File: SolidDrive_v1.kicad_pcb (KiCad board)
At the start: 2 copper layers, 50 x 70 mm, 13 parts, among them J1 Batt, M1 Motor_DC, Q1 NMOS, Q2 NMOS, Q3 NMOS, Q4 NMOS, U1 LM7805_TO220, U2 TLP250, U3 TLP250, U4 TLP250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

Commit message: [update] complete power cuircuit
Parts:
- added C3: 0.1μF, Capacitor_THT:C_Disc_D3.0mm_W1.6mm_P2.50mm, F.Cu at (67.5, 99.8)
- added C4: 0.1μF, Capacitor_THT:C_Disc_D3.0mm_W1.6mm_P2.50mm, F.Cu at (102.8, 100.2)
- added C5: 0.1μF, Capacitor_THT:C_Disc_D3.0mm_W1.6mm_P2.50mm, F.Cu at (67.2, 118.2)
- added C6: 0.1μF, Capacitor_THT:C_Disc_D3.0mm_W1.6mm_P2.50mm, F.Cu at (103.2, 117.8)
- added C7: 470μF, Capacitor_THT:CP_Radial_D5.0mm_P2.00mm, F.Cu at (52.8, 64.2)
- added C8: 470μF, Capacitor_THT:CP_Radial_D5.0mm_P2.00mm, F.Cu at (58.5, 64.2)
- added D1: 1N4007, Diode_THT:D_DO-41_SOD81_P10.16mm_Horizontal, F.Cu at (65.8, 84.0)
- added D2: 1N4007, Diode_THT:D_DO-41_SOD81_P10.16mm_Horizontal, F.Cu at (103.8, 83.8)
- added D3: 1N4007, Diode_THT:D_DO-41_SOD81_P10.16mm_Horizontal, F.Cu at (107.8, 101.5)
- added D4: 1N4007, Diode_THT:D_DO-41_SOD81_P10.16mm_Horizontal, F.Cu at (54.2, 102.0)
- added R1: R_PullDown, Resistor_THT:R_Axial_DIN0207_L6.3mm_D2.5mm_P10.16mm_Horizontal, F.Cu at (72.1, 92.8)
- added R2: R_PullDown, Resistor_THT:R_Axial_DIN0207_L6.3mm_D2.5mm_P10.16mm_Horizontal, F.Cu at (89.7, 93.2)
- added R3: R_PullDown, Resistor_THT:R_Axial_DIN0207_L6.3mm_D2.5mm_P10.16mm_Horizontal, F.Cu at (72.6, 96.2)
- added R4: R_PullDown, Resistor_THT:R_Axial_DIN0207_L6.3mm_D2.5mm_P10.16mm_Horizontal, F.Cu at (89.2, 96.8)
- added R5: R_Gate, Resistor_THT:R_Axial_DIN0207_L6.3mm_D2.5mm_P10.16mm_Horizontal, F.Cu at (68.8, 82.7)
- added R6: R_Gate, Resistor_THT:R_Axial_DIN0207_L6.3mm_D2.5mm_P10.16mm_Horizontal, F.Cu at (102.5, 86.8)
- added R7: R_Gate, Resistor_THT:R_Axial_DIN0207_L6.3mm_D2.5mm_P10.16mm_Horizontal, F.Cu at (68.5, 102.9)
- added R8: R_Gate, Resistor_THT:R_Axial_DIN0207_L6.3mm_D2.5mm_P10.16mm_Horizontal, F.Cu at (102.8, 103.9)
- moved M1 47.7 mm to (82.0, 65.0)
- moved C1 42.0 mm to (55.5, 71.0)
- moved Q2 41.3 mm to (95.0, 89.9), turned to 180 degrees
- moved J1 40.7 mm to (72.0, 65.0)
- moved Q4 40.6 mm to (90.0, 99.8)
- moved Q3 40.6 mm to (75.0, 99.5)
- moved Q1 38.9 mm to (80.0, 89.7), turned to 180 degrees
- moved C2 37.4 mm to (55.5, 81.0)
- moved U1 35.4 mm to (60.7, 76.0)
- moved U5 30.7 mm to (105.8, 105.5)
- moved U4 30.0 mm to (105.2, 87.4)
- moved U3 24.9 mm to (57.5, 105.2)
- moved U2 7.39 mm to (58.1, 87.8)
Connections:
- C1 pad 2: GND -> GNDPWR
- C2 pad 2: GND -> GNDPWR
- J1 pad 1: GND -> +BATT
- J1 pad 2: +BATT -> GNDPWR
- Q3 pad 3: GND -> GNDPWR
- Q4 pad 3: GND -> GNDPWR
- U1 pad 2: GND -> GNDPWR
- U2 pad 3: unconnected-(U2-C-Pad3) -> GND
- U2 pad 5: unconnected-(U2-VEE-Pad5) -> Net-(M1-+)
- U2 pad 6: unconnected-(U2-VO-Pad6) -> Net-(R5-Pad2)
- U2 pad 7: unconnected-(U2-VO-Pad7) -> Net-(R5-Pad2)
- U2 pad 8: unconnected-(U2-VCC-Pad8) -> Net-(D1-K)
- U3 pad 3: unconnected-(U3-C-Pad3) -> GND
- U3 pad 5: unconnected-(U3-VEE-Pad5) -> GNDPWR
- U3 pad 6: unconnected-(U3-VO-Pad6) -> Net-(R6-Pad2)
- U3 pad 7: unconnected-(U3-VO-Pad7) -> Net-(R6-Pad2)
- U3 pad 8: unconnected-(U3-VCC-Pad8) -> Net-(D3-K)
- U4 pad 3: unconnected-(U4-C-Pad3) -> GND
- U4 pad 5: unconnected-(U4-VEE-Pad5) -> Net-(M1--)
- U4 pad 6: unconnected-(U4-VO-Pad6) -> Net-(R8-Pad1)
- U4 pad 7: unconnected-(U4-VO-Pad7) -> Net-(R8-Pad1)
- U4 pad 8: unconnected-(U4-VCC-Pad8) -> Net-(D2-K)
- U5 pad 3: unconnected-(U5-C-Pad3) -> GND
- U5 pad 5: unconnected-(U5-VEE-Pad5) -> GNDPWR
- U5 pad 6: unconnected-(U5-VO-Pad6) -> Net-(R7-Pad1)
- U5 pad 7: unconnected-(U5-VO-Pad7) -> Net-(R7-Pad1)
- U5 pad 8: unconnected-(U5-VCC-Pad8) -> Net-(D4-K)
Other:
- board size 50 x 70 mm -> 70 x 70 mm

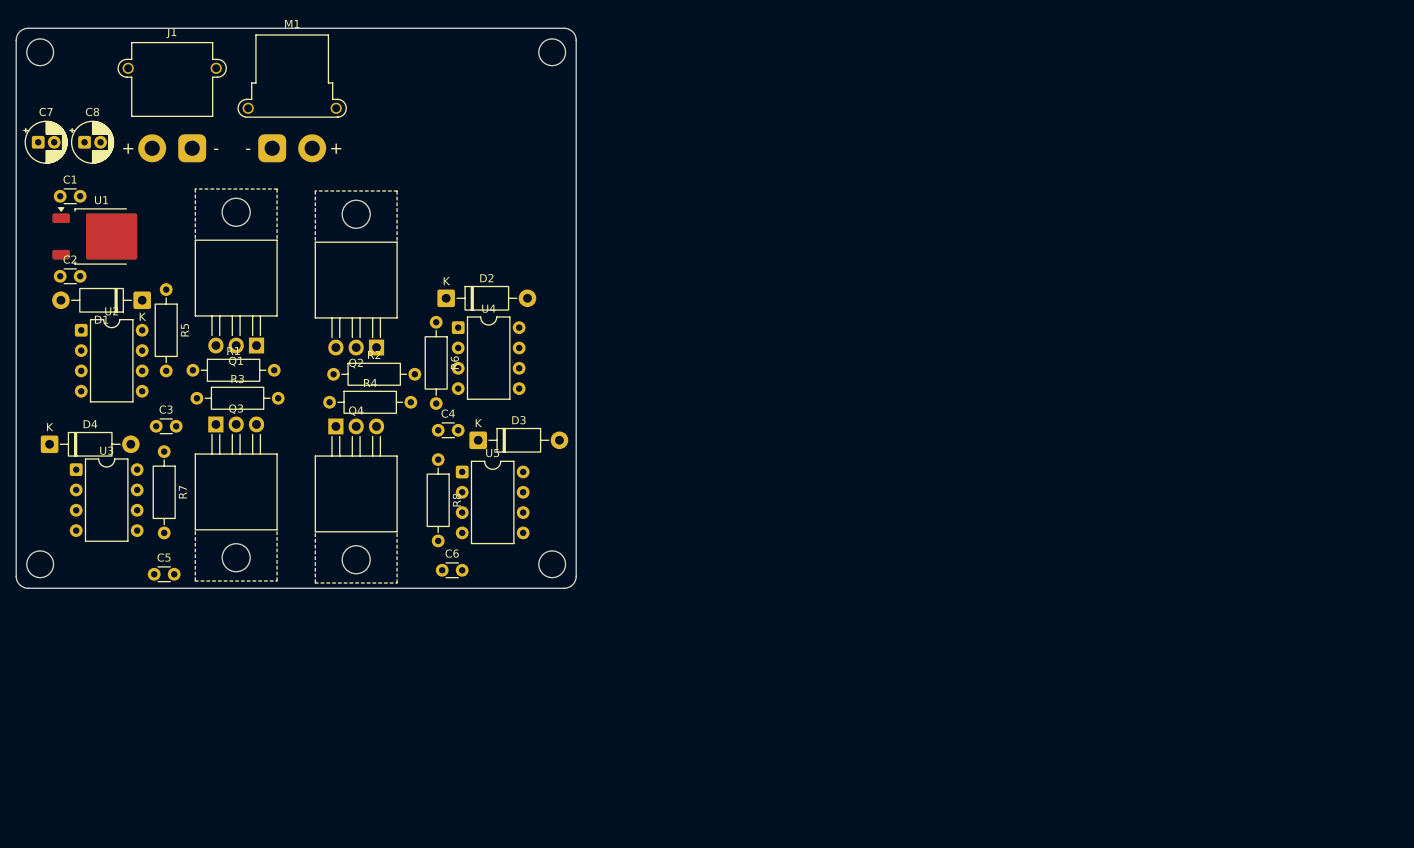
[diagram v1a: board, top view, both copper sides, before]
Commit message: [update] complete logic circuit
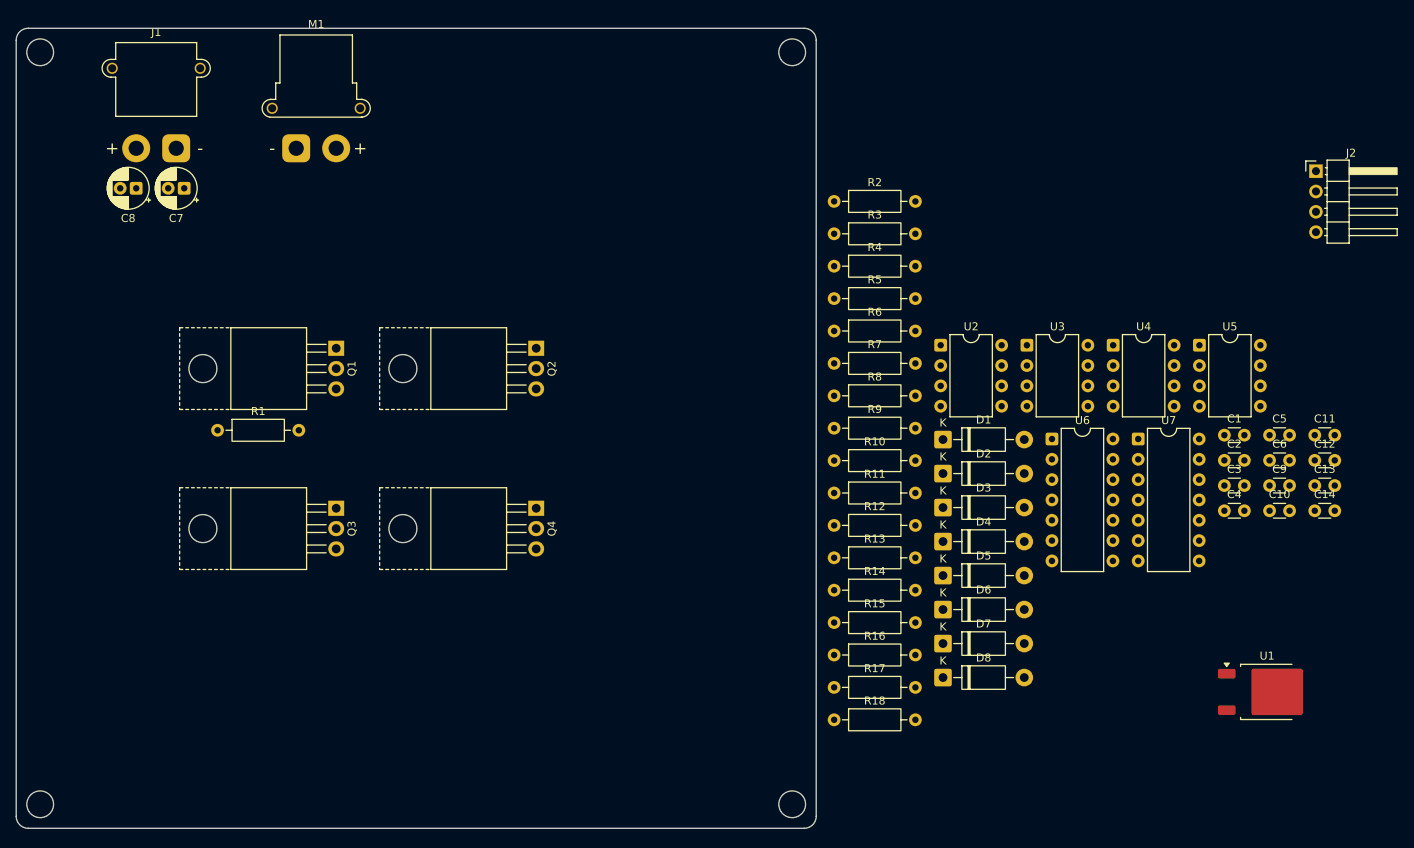
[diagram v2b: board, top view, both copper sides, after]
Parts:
- added C10: C_Delay, Capacitor_THT:C_Disc_D3.0mm_W1.6mm_P2.50mm, F.Cu at (206.7, 110.3)
- added C11: C_Delay, Capacitor_THT:C_Disc_D3.0mm_W1.6mm_P2.50mm, F.Cu at (212.3, 100.9)
- added C12: C_Delay, Capacitor_THT:C_Disc_D3.0mm_W1.6mm_P2.50mm, F.Cu at (212.3, 104.0)
- added C13: 0.1μF, Capacitor_THT:C_Disc_D3.0mm_W1.6mm_P2.50mm, F.Cu at (212.3, 107.2)
- added C14: 0.1μF, Capacitor_THT:C_Disc_D3.0mm_W1.6mm_P2.50mm, F.Cu at (212.3, 110.3)
- added C9: C_Delay, Capacitor_THT:C_Disc_D3.0mm_W1.6mm_P2.50mm, F.Cu at (206.7, 107.2)
- added D5: 1N4007, Diode_THT:D_DO-41_SOD81_P10.16mm_Horizontal, F.Cu at (165.8, 118.4)
- added D6: 1N4007, Diode_THT:D_DO-41_SOD81_P10.16mm_Horizontal, F.Cu at (165.8, 122.7)
- added D7: 1N4007, Diode_THT:D_DO-41_SOD81_P10.16mm_Horizontal, F.Cu at (165.8, 126.9)
- added D8: 1N4007, Diode_THT:D_DO-41_SOD81_P10.16mm_Horizontal, F.Cu at (165.8, 131.2)
- added J2: control_input, Connector_PinHeader_2.54mm:PinHeader_1x04_P2.54mm_Horizontal, F.Cu at (212.5, 67.9)
- added R10: R_tlp, Resistor_THT:R_Axial_DIN0207_L6.3mm_D2.5mm_P10.16mm_Horizontal, F.Cu at (152.2, 104.0)
- added R11: R_tlp, Resistor_THT:R_Axial_DIN0207_L6.3mm_D2.5mm_P10.16mm_Horizontal, F.Cu at (152.2, 108.1)
- added R12: R_tlp, Resistor_THT:R_Axial_DIN0207_L6.3mm_D2.5mm_P10.16mm_Horizontal, F.Cu at (152.2, 112.1)
- added R13: R_PullDown, Resistor_THT:R_Axial_DIN0207_L6.3mm_D2.5mm_P10.16mm_Horizontal, F.Cu at (152.2, 116.2)
- added R14: R_PullDown, Resistor_THT:R_Axial_DIN0207_L6.3mm_D2.5mm_P10.16mm_Horizontal, F.Cu at (152.2, 120.2)
- added R15: R_Delay, Resistor_THT:R_Axial_DIN0207_L6.3mm_D2.5mm_P10.16mm_Horizontal, F.Cu at (152.2, 124.3)
- added R16: R_Delay, Resistor_THT:R_Axial_DIN0207_L6.3mm_D2.5mm_P10.16mm_Horizontal, F.Cu at (152.2, 128.3)
- added R17: R_Delay, Resistor_THT:R_Axial_DIN0207_L6.3mm_D2.5mm_P10.16mm_Horizontal, F.Cu at (152.2, 132.4)
- added R18: R_Delay, Resistor_THT:R_Axial_DIN0207_L6.3mm_D2.5mm_P10.16mm_Horizontal, F.Cu at (152.2, 136.4)
- added R9: R_tlp, Resistor_THT:R_Axial_DIN0207_L6.3mm_D2.5mm_P10.16mm_Horizontal, F.Cu at (152.2, 100.0)
- added U6: 74HC00, Package_DIP:DIP-14_W7.62mm, F.Cu at (179.5, 101.3)
- added U7: 74HC14, Package_DIP:DIP-14_W7.62mm, F.Cu at (190.2, 101.3)
- moved U1 156.4 mm to (206.4, 133.0)
- moved C1 148.6 mm to (201.0, 100.9)
- moved C2 147.3 mm to (201.0, 104.0)
- moved C5 140.5 mm to (206.7, 100.9)
- moved C3 133.7 mm to (201.0, 107.2)
- moved U3 119.9 mm to (176.3, 89.6)
- moved D4 112.3 mm to (165.8, 114.2)
- moved U2 107.4 mm to (165.6, 89.6)
- moved C6 104.3 mm to (206.7, 104.0)
- moved D1 101.6 mm to (165.8, 101.4), turned to 0 degrees
- moved C4 98.8 mm to (201.0, 110.3)
- moved U5 93.5 mm to (197.9, 89.6)
- moved R7 84.5 mm to (152.2, 91.9), turned to 0 degrees
- moved R5 83.5 mm to (152.2, 83.8), turned to 0 degrees
- moved R3 82.3 mm to (152.2, 75.7)
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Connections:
- U2 pad 2: unconnected-(U2-A-Pad2) -> Net-(U2-A)
- U3 pad 2: unconnected-(U3-A-Pad2) -> Net-(U3-A)
- U4 pad 2: unconnected-(U4-A-Pad2) -> Net-(U4-A)
- U5 pad 2: unconnected-(U5-A-Pad2) -> Net-(U5-A)
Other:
- board size 70 x 70 mm -> 100 x 100 mm

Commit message: [update] complete logic circuit placement
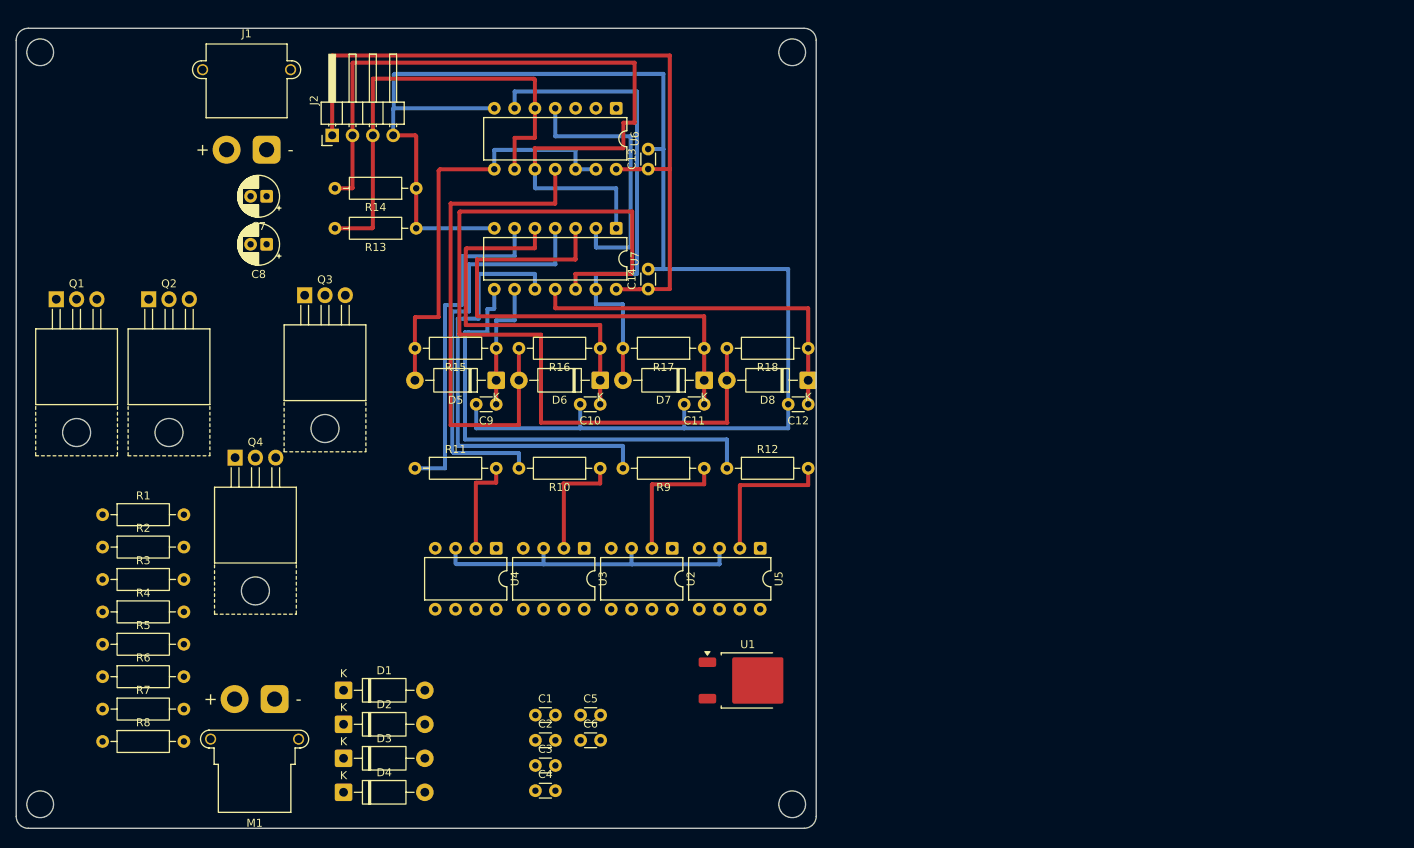
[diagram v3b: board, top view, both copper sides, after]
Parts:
- moved J2 123.1 mm to (89.5, 63.4), turned to 90 degrees
- moved R2 101.1 mm to (60.8, 114.8)
- moved R3 101.1 mm to (60.8, 118.9)
- moved R4 101.1 mm to (60.8, 123.0)
- moved R5 101.1 mm to (60.8, 127.0)
- moved R6 101.1 mm to (60.8, 131.1)
- moved R7 101.1 mm to (60.8, 135.1)
- moved R8 101.1 mm to (60.8, 139.2)
- moved C9 97.2 mm to (110.0, 97.0), turned to 180 degrees
- moved C1 93.0 mm to (114.9, 135.8)
- moved C2 93.0 mm to (114.9, 139.0)
- moved C3 93.0 mm to (114.9, 142.2)
- moved C4 93.0 mm to (114.9, 145.3)
- moved C5 93.0 mm to (120.5, 135.8)
- moved C6 93.0 mm to (120.5, 139.0)
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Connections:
- U7 pad 1: Net-(D8-K) -> DIR
- U7 pad 10: Net-(U6-Pad4) -> input1
- U7 pad 11: DIR -> Net-(D8-K)
- U7 pad 2: input1 -> Net-(U6-Pad4)
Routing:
- net GND: track 0.00 -> 230.7 mm
- net Net-(D8-A): track 0.00 -> 107.5 mm
- net DIR: track 0.00 -> 96.4 mm
- net +3.3V: track 0.00 -> 94.8 mm
- net Net-(D6-A): track 0.00 -> 63.2 mm
- net Net-(D7-K): track 0.00 -> 62.6 mm
- net Net-(D7-A): track 0.00 -> 61.9 mm
- net input4: track 0.00 -> 58.7 mm
- net PWM: track 0.00 -> 57.4 mm
- net input1: track 0.00 -> 56.5 mm
- net Net-(D5-A): track 0.00 -> 53.7 mm
- net input2: track 0.00 -> 51.1 mm
- net Net-(D6-K): track 0.00 -> 47.4 mm
- net Net-(D8-K): track 0.00 -> 46.0 mm
- net input3: track 0.00 -> 42.5 mm
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
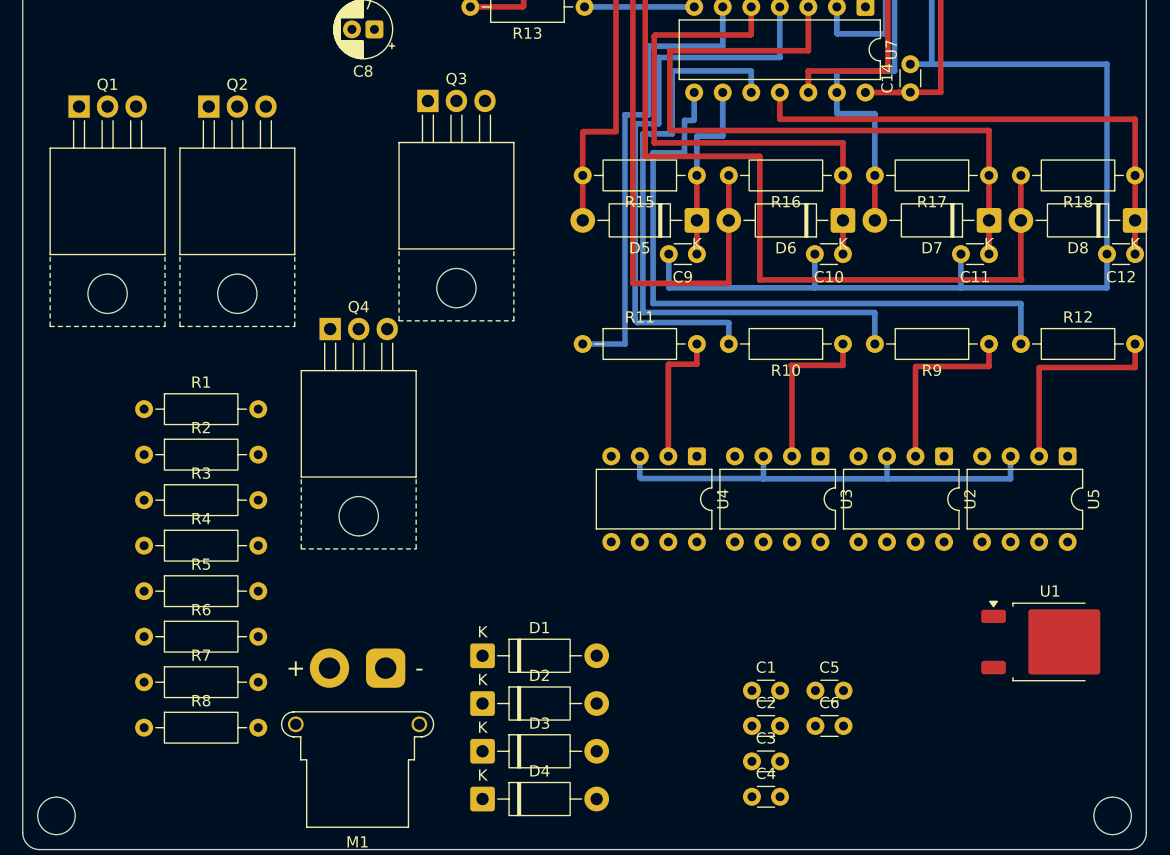
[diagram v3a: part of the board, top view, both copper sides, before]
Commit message: [update] complete gate driver placement
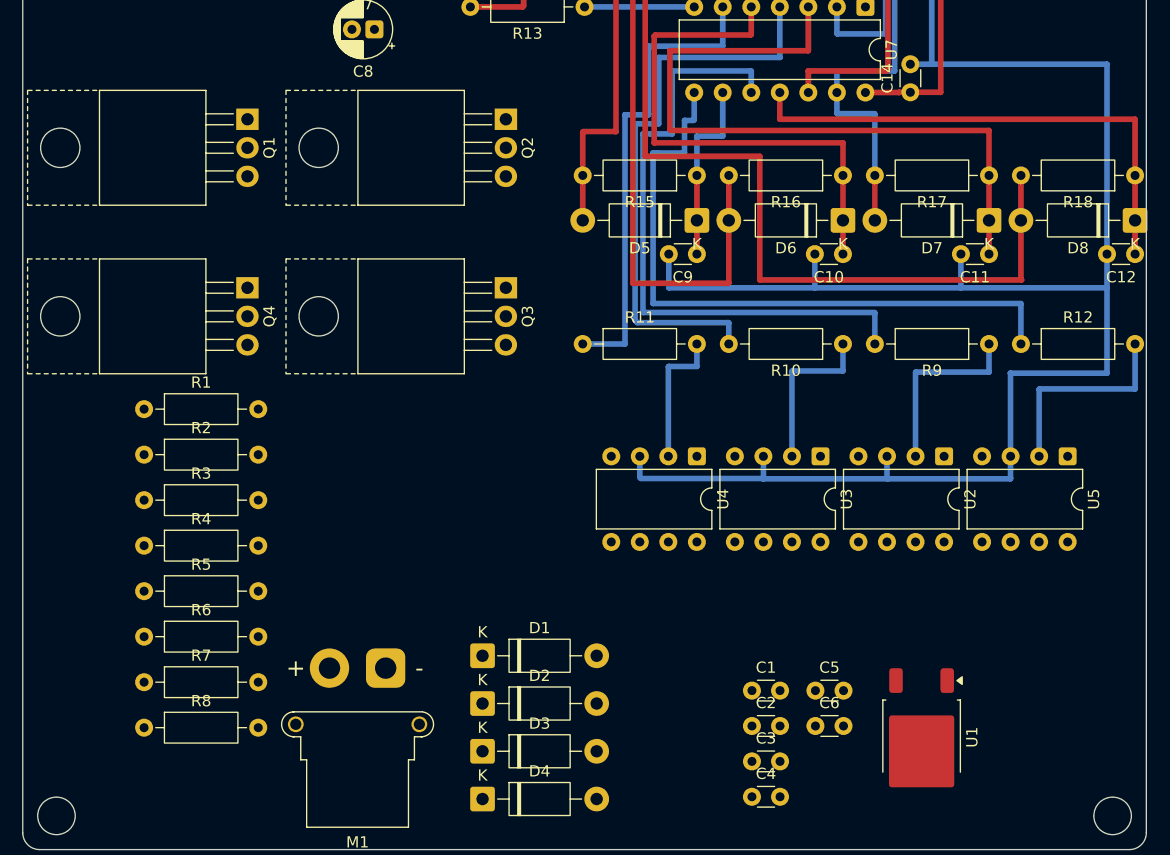
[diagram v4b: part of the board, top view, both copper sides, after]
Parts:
- moved Q2 26.5 mm to (93.0, 85.0), turned to -90 degrees
- moved Q3 18.0 mm to (93.0, 100.0), turned to -90 degrees
- moved Q1 15.0 mm to (70.0, 85.0), turned to -90 degrees
- moved U1 14.2 mm to (130.0, 140.0), turned to -90 degrees
- moved Q4 8.22 mm to (70.0, 100.0), turned to -90 degrees
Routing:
- net GND: track 230.7 -> 254.3 mm

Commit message: [udpate] complete part position
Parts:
- added 3.3V: LED, LED_THT:LED_D3.0mm, F.Cu at (134.2, 77.5)
- added Battery: LED, LED_THT:LED_D3.0mm, F.Cu at (140.6, 77.4)
- added R19: 1kΩ, Resistor_THT:R_Axial_DIN0207_L6.3mm_D2.5mm_P10.16mm_Horizontal, F.Cu at (140.9, 62.0)
- added R20: 120, Resistor_THT:R_Axial_DIN0207_L6.3mm_D2.5mm_P10.16mm_Horizontal, F.Cu at (136.9, 62.0)
- C7, C8: footprint Capacitor_THT:CP_Radial_D5.0mm_P2.00mm -> Capacitor_THT:CP_Radial_D10.0mm_P7.50mm
- moved D4 56.0 mm to (143.1, 125.2), turned to -90 degrees
- moved R8 47.4 mm to (82.7, 97.1)
- moved D1 41.7 mm to (131.9, 125.3), turned to -90 degrees
- moved D3 34.1 mm to (121.1, 125.3), turned to -90 degrees
- moved R5 30.5 mm to (59.9, 96.5)
- moved R2 26.2 mm to (83.0, 101.0)
- moved R6 24.2 mm to (82.7, 120.8)
- moved R3 23.0 mm to (82.7, 125.6)
- moved C4 22.6 mm to (105.0, 125.0), turned to 180 degrees
- moved D2 22.4 mm to (110.0, 125.3), turned to -90 degrees
- moved C6 22.3 mm to (137.8, 124.9), turned to 180 degrees
- moved C3 20.9 mm to (126.8, 125.0), turned to 180 degrees
- moved R7 14.4 mm to (59.8, 120.8)
- moved R1 13.1 mm to (70.0, 101.5), turned to 180 degrees
- moved C7 12.5 mm to (69.4, 75.0)
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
